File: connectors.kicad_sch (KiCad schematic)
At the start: 57 parts, among them J1 Molex_Nano-Fit_1x2_SMD_105430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, J2 Conn_FAKRA_59S2AQ-40MT5-Z_1, J3 Conn_FAKRA_59S2AQ-40MT5-Z_1, J4 Conn_FAKRA_59S2AQ-40MT5-Z_1, J5 Conn_FAKRA_59S2AQ-40MT5-Z_1, J6 Conn_FFC_WE_68715014522, U1 SN74LV1T125DBVR, U2 SN74LV1T125DBVR, U8 NTS0102_TSSOP

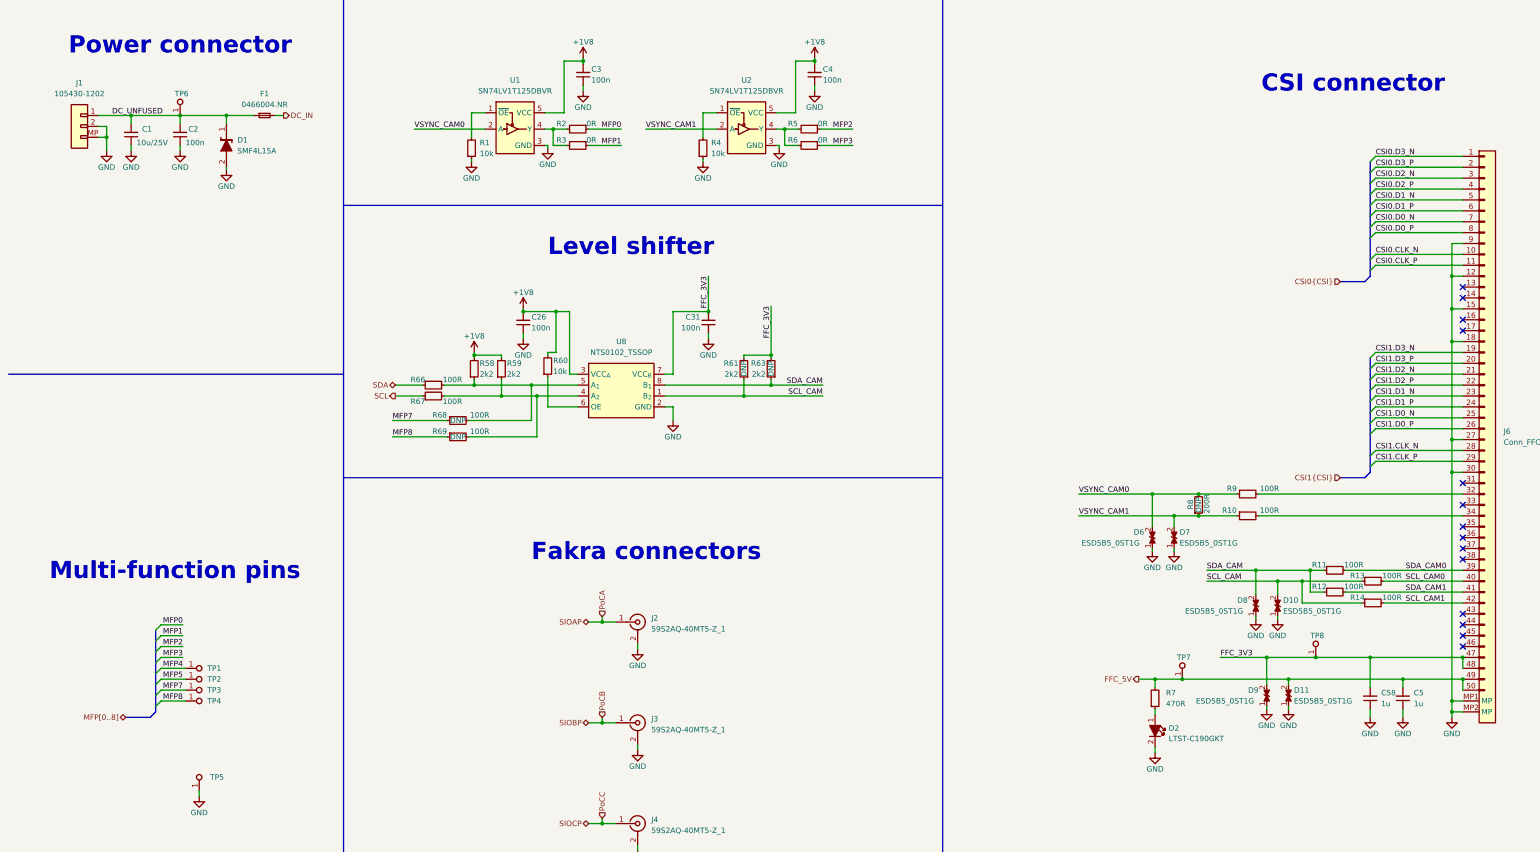
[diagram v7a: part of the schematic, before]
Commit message: Clean ERC, move LED from 5V to 12V
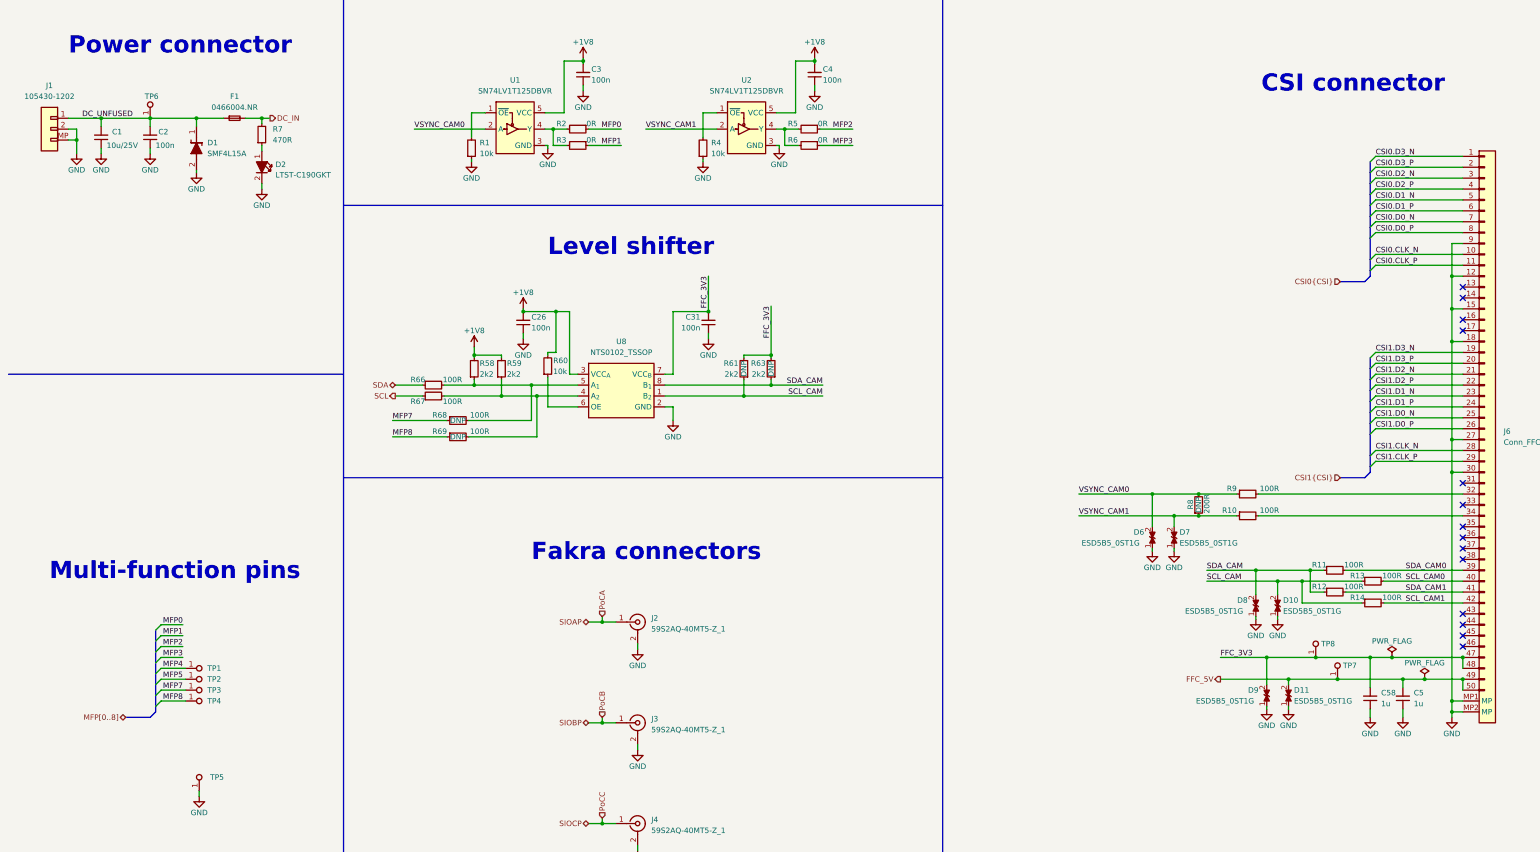
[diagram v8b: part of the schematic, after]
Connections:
- net DC_IN: now also R7.2
- net FFC_5V: no longer R7.2
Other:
- moved on the sheet: C1, C2, D1, F1, J1, TP6, TP7
